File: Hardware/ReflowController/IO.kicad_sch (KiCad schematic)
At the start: 0 parts

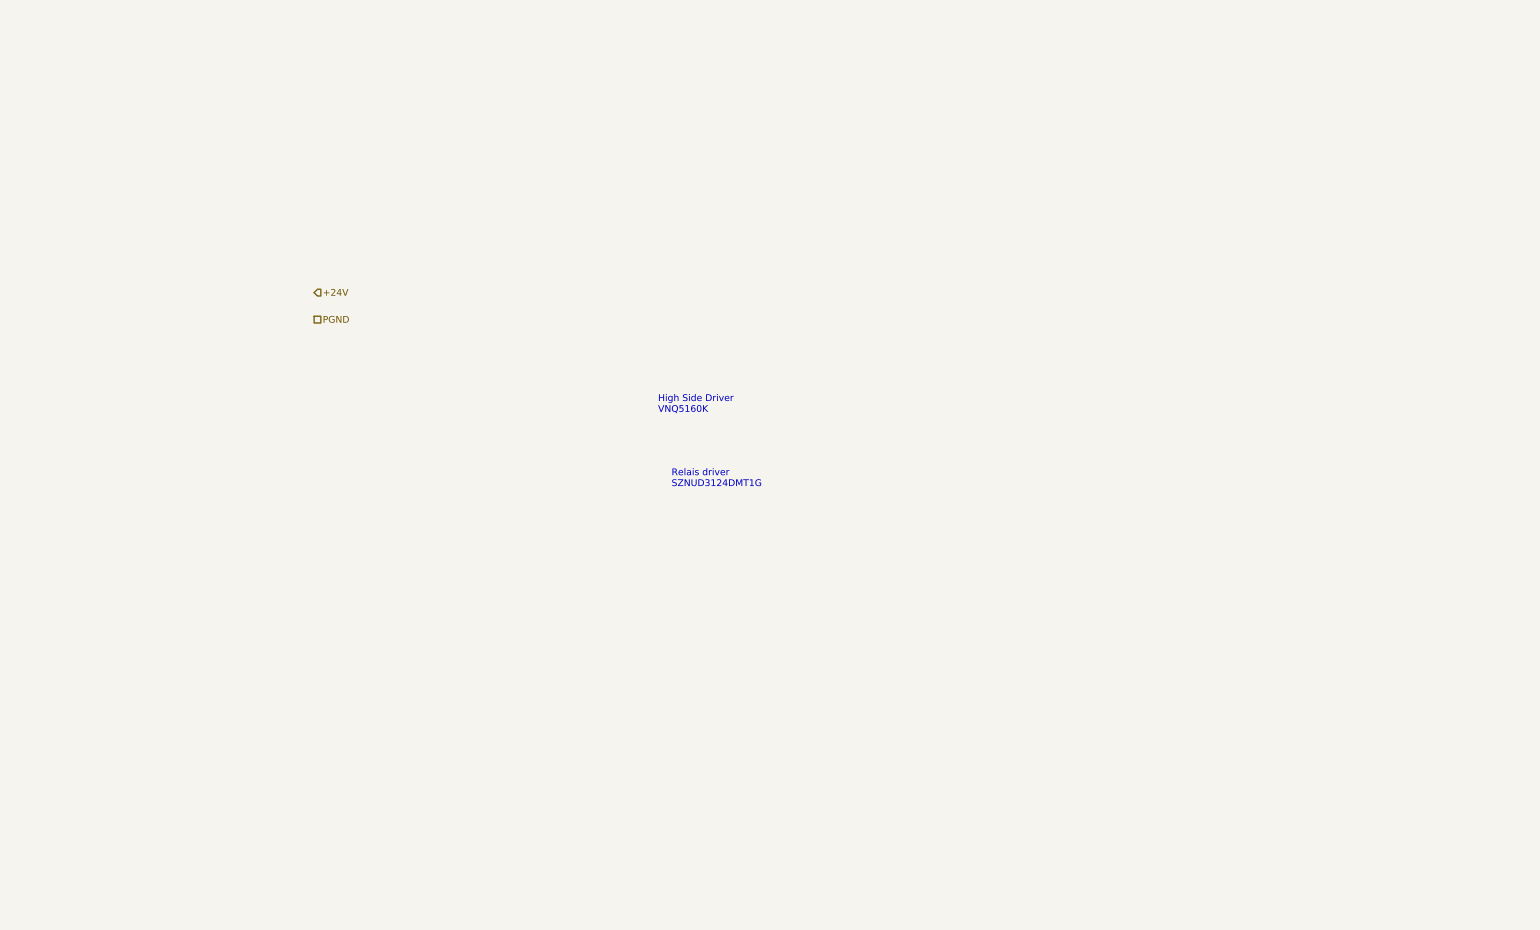
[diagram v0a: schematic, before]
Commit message: IMplemented the relay driver and High side switch. For the HSS there are some values to be caculated to enhance safety measures if we decide to implment them
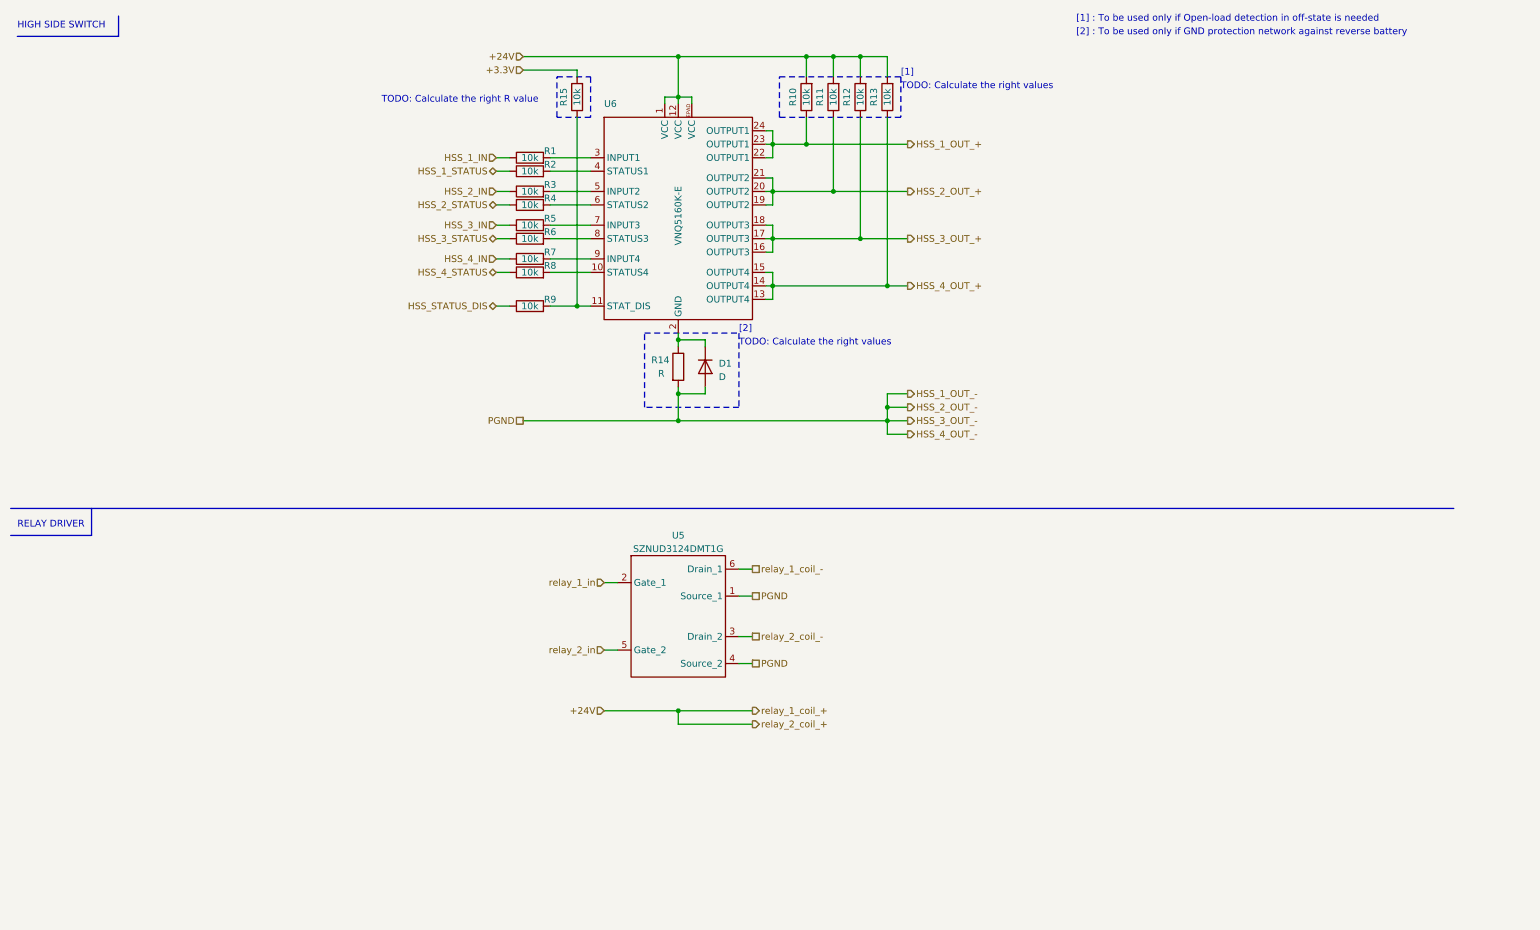
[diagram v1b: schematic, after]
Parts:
- added D1: D, symbol Device:D
- added R1, R10, R11, R12, R13, R15, R2, R3, R4, R5, R6, R7, R8, R9: 10k, Resistor_SMD:R_0603_1608Metric_Pad0.98x0.95mm_HandSolder, symbol Device:R
- added R14: R, symbol Device:R
- added U5: SZNUD3124DMT1G, Package_SO:SC-74-6_1.5x2.9mm_P0.95mm, symbol 180_active_driver_relay:SZNUD3124DMT1G
- added U6: VNQ5160K-E, 190_active_high_side_switches:VNQ5160K-E, symbol 190_active_high_side_switches:VNQ5160K
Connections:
- net +24V: now also R10.2, R11.2, R12.2, R13.2, U6.1 (VCC), U6.12 (VCC), U6.EPAD (VCC)
- new net: R5.2, U6.7 (INPUT3)
- new net: R8.2, U6.10 (STATUS4)
- new net: R15.1, R9.2, U6.11 (STAT_DIS)
- new net: D1.1 (K), R14.1, U6.2 (GND)
- new net: R1.2, U6.3 (INPUT1)
- new net: R2.2, U6.4 (STATUS1)
- new net: R3.2, U6.5 (INPUT2)
- new net: R4.2, U6.6 (STATUS2)
- new net: R6.2, U6.8 (STATUS3)
- new net: R7.2, U6.9 (INPUT4)
- new net +3.3V: R15.2
- new net HSS_1_IN: R1.1
- new net HSS_1_OUT_+: R10.1, U6.22 (OUTPUT1), U6.23 (OUTPUT1), U6.24 (OUTPUT1)
- new net HSS_1_OUT_-: D1.2 (A), R14.2, U5.1 (Source_1), U5.4 (Source_2)
- new net HSS_1_STATUS: R2.1
- new net HSS_2_IN: R3.1
- new net HSS_2_OUT_+: R11.1, U6.19 (OUTPUT2), U6.20 (OUTPUT2), U6.21 (OUTPUT2)
- new net HSS_2_STATUS: R4.1
- new net HSS_3_IN: R5.1
- new net HSS_3_OUT_+: R12.1, U6.16 (OUTPUT3), U6.17 (OUTPUT3), U6.18 (OUTPUT3)
- new net HSS_3_STATUS: R6.1
- new net HSS_4_IN: R7.1
- new net HSS_4_OUT_+: R13.1, U6.13 (OUTPUT4), U6.14 (OUTPUT4), U6.15 (OUTPUT4)
- new net HSS_4_STATUS: R8.1
- new net HSS_STATUS_DIS: R9.1
- new net relay_1_coil_-: U5.6 (Drain_1)
- new net relay_1_in: U5.2 (Gate_1)
- new net relay_2_coil_-: U5.3 (Drain_2)
- new net relay_2_in: U5.5 (Gate_2)
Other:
- note added: "HIGH SIDE SWITCH"
- note added: "RELAY DRIVER"
- note added: "TODO: Calculate the right R value"
- note added: "TODO: Calculate the right values"
- note added: "[1]"
- note added: "[1] : To be used only if Open-load detection in off-state is needed"
- note added: "[2]"
- note added: "[2] : To be used only if GND protection network against reverse battery"
- note removed: "High Side Driver VNQ5160K"
- note removed: "Relais driver SZNUD3124DMT1G"

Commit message: Finished the fan controllers calculations, added the wago connectors, added notes
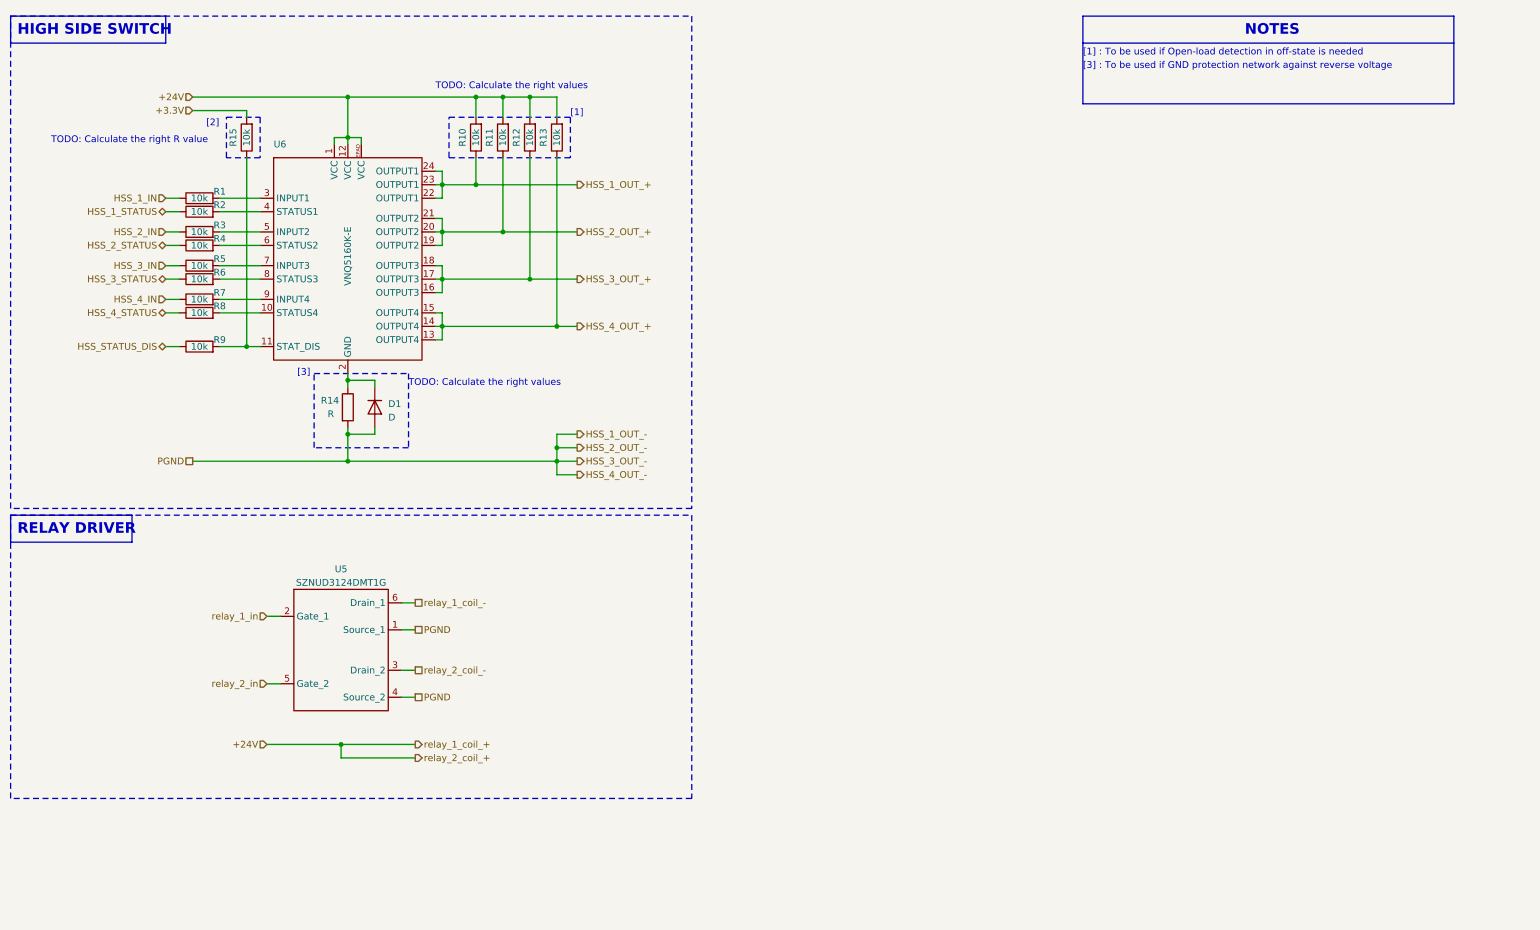
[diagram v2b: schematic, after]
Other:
- note added: "NOTES"
- note added: "[1] : To be used if Open-load detection in off-state is needed"
- note added: "[3]"
- note added: "[3] : To be used if GND protection network against reverse voltage"
- note removed: "[1] : To be used only if Open-load detection in off-state is needed"
- note removed: "[2] : To be used only if GND protection network against reverse battery"
- title: (none) -> Reflow Oven Control
- moved on the sheet: D1, R1, R10, R11, R12, R13, R14, R15, R2, R3, R4, R5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
